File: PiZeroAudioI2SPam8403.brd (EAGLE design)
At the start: 65.1 x 30.2 mm, 60 parts, among them CON1 RPI-ZERO, J1 GROVE, J2 2X2HEADER, J3 JST, J4 AMP FCI 10103594-0001LF, J5 2X1-LOCKING, J6 GROVE, J7 4X1-LOCKING, Q1 DMG2305UX, U1 TXB0104PWR, U2 LSM6DS33, U3 PCM5101A, U4 MCP73831, U5 DMMT5401, U6 TXS0102, U7 PAM8403, U8 PAM2401

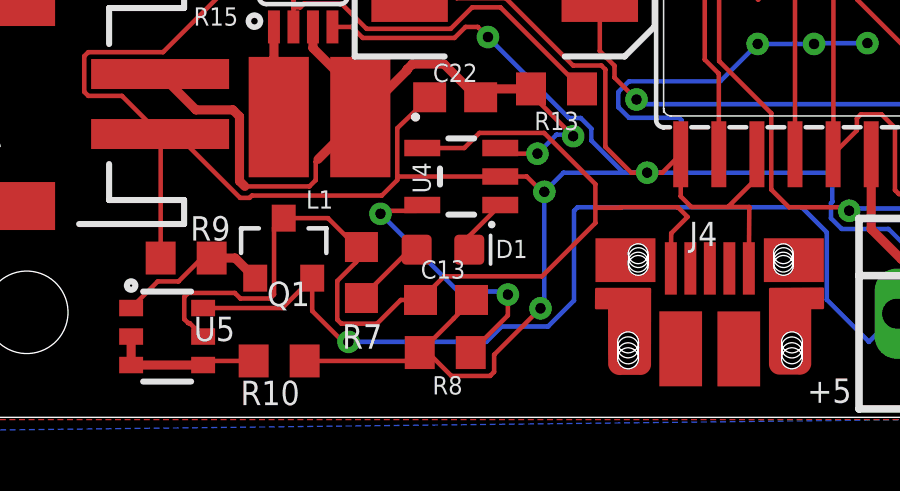
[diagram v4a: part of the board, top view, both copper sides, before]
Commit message: Updated Capacitor footprint
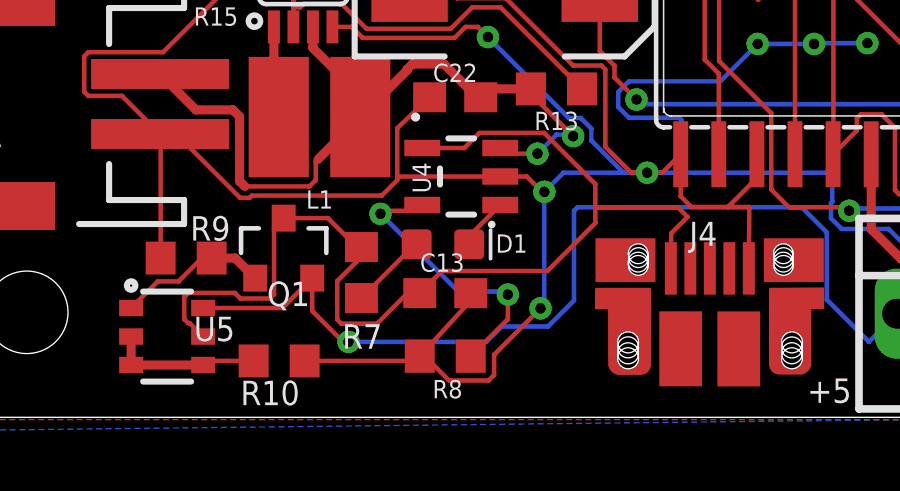
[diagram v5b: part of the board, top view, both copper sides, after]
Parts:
- C13: device SparkFun-Capacitors:0603 -> rcl:C0603
- moved C13 0.23 mm to (-61.3, 5.41)
- moved D1 0.18 mm to (-61.4, 7.04)
- moved R8 0.13 mm to (-61.3, 3.30)
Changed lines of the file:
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@@
 <attribute name="VALUE" x="-56.6928" y="17.6276" size="1.27" layer="27"/>
 </element>
-<element name="C13" library="SparkFun-Capacitors" package="0603" value="4.7uF" x="-61.2648" y="5.1816" smashed="yes">
-<attribute name="NAME" x="-61.3664" y="5.8928" size="0.6096" layer="25" ratio="20" align="bottom-center"/>
-<attribute name="PROD_ID" value="CAP-08280" x="-82.2706" y="27.7622" size="1.778" layer="27" display="off"/>
-<attribute name="VALUE" x="-61.2648" y="4.4196" size="0.6096" layer="27" font="vector" ratio="20" align="top-center"/>
+<element name="C13" library="rcl" library_urn="urn:adsk.eagle:library:334" package="C0603" package3d_urn="urn:adsk.eagle:package:23616/2" value="4.7uF" x="-61.2902" y="5.4102" smashed="yes">
+<attribute name="NAME" x="-61.3918" y="6.1214" size="0.6096" layer="25" ratio="20" align="bottom-center"/>
+<attribute name="SPICEPREFIX" value="C" x="-61.2902" y="5.4102" size="1.778" layer="27" display="off"/>
 </element>
-<element name="D1" library="SparkFun-LED" package="LED-0603" value="BLUE" x="-61.3664" y="6.858" smashed="yes">
-<attribute name="NAME" x="-59.0804" y="6.5786" size="0.6096" layer="25" ratio="20" align="bottom-center"/>
-<attribute name="PROD_ID" value="DIO-08575" x="-73.9902" y="26.8732" size="1.778" layer="27" display="off"/>
-<attribute name="VALUE" x="-61.3664" y="6.223" size="0.6096" layer="27" font="vector" ratio="20" align="top-center"/>
+<element name="D1" library="SparkFun-LED" package="LED-0603" value="BLUE" x="-61.3664" y="7.0358" smashed="yes">
+<attribute name="NAME" x="-59.0804" y="6.7564" size="0.6096" layer="25" ratio="20" align="bottom-center"/>
+<attribute name="PROD_ID" value="DIO-08575" x="-73.9902" y="27.051" size="1.778" layer="27" display="off"/>
+<attribute name="VALUE" x="-61.3664" y="6.4008" size="0.6096" layer="27" font="vector" ratio="20" align="top-center"/>
 </element>
 <element name="R7" library="adafruit" package="R0603" value="1k" x="-64.0842" y="6.096" smashed="yes" rot="R90">
 <attribute name="NAME" x="-64.0588" y="4.3688" size="0.8128" layer="25" ratio="20" rot="R180" align="bottom-center"/>
 </element>
-<element name="R8" library="adafruit" package="R0603" value="2.0k" x="-61.2902" y="3.429" smashed="yes" rot="R180">
-<attribute name="NAME" x="-61.214" y="2.6416" size="0.6096" layer="25" ratio="20" rot="R180" align="bottom-center"/>
+<element name="R8" library="adafruit" package="R0603" value="2.0k" x="-61.2902" y="3.302" smashed="yes" rot="R180">
+<attribute name="NAME" x="-61.214" y="2.5146" size="0.6096" layer="25" ratio="20" rot="R180" align="bottom-center"/>
 </element>
 <element name="U4" library="SparkFun-IC-Power" package="SOT23-5" value="MCP73831" x="-60.7568" y="9.2964" smashed="yes" rot="R90">
@@
 <wire x1="-62.8904" y1="9.1763125" x2="-63.4053125" y2="8.6614" width="0.1524" layer="1"/>
 <wire x1="-63.4053125" y1="8.6614" x2="-67.73563125" y2="8.6614" width="0.1524" layer="1"/>
-<wire x1="-60.4148" y1="5.1816" x2="-60.5434125" y2="5.0470875" width="0.1524" layer="1"/>
-<wire x1="-60.5434125" y1="5.0470875" x2="-61.0076375" y2="4.5615625" width="0.1524" layer="1"/>
-<wire x1="-61.0076375" y1="4.5615625" x2="-62.1402" y2="3.429" width="0.1524" layer="1"/>
-<wire x1="-60.4148" y1="5.1816" x2="-60.5434125" y2="5.0529875" width="0.1524" layer="1"/>
-<wire x1="-60.5434125" y1="5.0529875" x2="-60.5434125" y2="5.0470875" width="0.1524" layer="1"/>
-<wire x1="-65.9774" y1="3.1496" x2="-62.4196" y2="3.1496" width="0.1524" layer="1"/>
-<wire x1="-62.4196" y1="3.1496" x2="-62.1402" y2="3.429" width="0.1524" layer="1"/>
+<wire x1="-60.5434125" y1="5.0470875" x2="-60.579865625" y2="5.0089625" width="0.1524" layer="1"/>
+<wire x1="-60.579865625" y1="5.0089625" x2="-62.1402" y2="3.302" width="0.1524" layer="1"/>
+<wire x1="-60.4402" y1="5.4102" x2="-60.5434125" y2="5.3069875" width="0.1524" layer="1"/>
+<wire x1="-60.5434125" y1="5.3069875" x2="-60.5434125" y2="5.0470875" width="0.1524" layer="1"/>
+<wire x1="-65.9774" y1="3.1496" x2="-62.2926" y2="3.1496" width="0.1524" layer="1"/>
+<wire x1="-62.2926" y1="3.1496" x2="-62.1402" y2="3.302" width="0.1524" layer="1"/>
 <wire x1="-59.4567" y1="9.2964" x2="-62.865" y2="9.2964" width="0.1524" layer="1"/>
 <wire x1="-62.865" y1="9.2964" x2="-62.8904" y2="9.271" width="0.1524" layer="1"/>
@@
 <wire x1="-55.9532" y1="12.8628875" x2="-55.9532" y2="10.284" width="0.1524" layer="1"/>
 <via x="-58.1152" y="4.9022" extent="1-16" drill="0.35"/>
-<wire x1="-61.0848875" y1="2.6496" x2="-59.7955125" y2="2.6496" width="0.1524" layer="1"/>
-<wire x1="-59.7955125" y1="2.6496" x2="-59.6616" y2="2.7835125" width="0.1524" layer="1"/>
-<wire x1="-62.1402" y1="3.429" x2="-61.8642875" y2="3.429" width="0.1524" layer="1"/>
-<wire x1="-59.6616" y1="2.7835125" x2="-59.6616" y2="3.3558" width="0.1524" layer="1"/>
-<wire x1="-61.8642875" y1="3.429" x2="-61.0848875" y2="2.6496" width="0.1524" layer="1"/>
+<wire x1="-61.1610875" y1="2.4972" x2="-59.8463125" y2="2.4972" width="0.1524" layer="1"/>
+<wire x1="-59.8463125" y1="2.4972" x2="-59.6616" y2="2.6819125" width="0.1524" layer="1"/>
+<wire x1="-62.1402" y1="3.302" x2="-61.9658875" y2="3.302" width="0.1524" layer="1"/>
+<wire x1="-59.6616" y1="2.6819125" x2="-59.6616" y2="3.3558" width="0.1524" layer="1"/>
+<wire x1="-61.9658875" y1="3.302" x2="-61.1610875" y2="2.4972" width="0.1524" layer="1"/>
 <wire x1="-59.6616" y1="3.3558" x2="-58.1152" y2="4.9022" width="0.1524" layer="1"/>
 <wire x1="-58.1152" y1="4.9022" x2="-57.9882" y2="5.0292" width="0.1524" layer="16"/>
@@
 <wire x1="-59.2074" y1="5.366653125" x2="-59.202946875" y2="5.3622" width="0.1524" layer="16"/>
 <via x="-59.202946875" y="5.3622" extent="1-16" drill="0.35"/>
-<wire x1="-59.202946875" y1="5.3622" x2="-59.202946875" y2="4.666253125" width="0.1524" layer="1"/>
-<wire x1="-59.202946875" y1="4.666253125" x2="-60.4402" y2="3.429" width="0.1524" layer="1"/>
+<wire x1="-59.202946875" y1="5.3622" x2="-59.202946875" y2="4.539253125" width="0.1524" layer="1"/>
+<wire x1="-59.202946875" y1="4.539253125" x2="-60.4402" y2="3.302" width="0.1524" layer="1"/>
 <wire x1="-62.2499" y1="8.1534" x2="-63.3504" y2="8.1534" width="0.1524" layer="1"/>
 </signal>
@@
 <contactref element="D1" pad="C"/>
 <wire x1="-59.4567" y1="8.3464" x2="-60.4894" y2="7.3137" width="0.1524" layer="1"/>
-<wire x1="-60.4894" y1="7.3137" x2="-60.4894" y2="6.858" width="0.1524" layer="1"/>
+<wire x1="-60.4894" y1="7.3137" x2="-60.4894" y2="7.0358" width="0.1524" layer="1"/>
 </signal>
 <signal name="EN">
@@
 <contactref element="R7" pad="1"/>
 <contactref element="D1" pad="A"/>
-<wire x1="-62.2434" y1="6.858" x2="-62.4722" y2="6.858" width="0.1524" layer="1"/>
-<wire x1="-62.4722" y1="6.858" x2="-64.0842" y2="5.246" width="0.1524" layer="1"/>
+<wire x1="-62.2434" y1="7.0358" x2="-62.2944" y2="7.0358" width="0.1524" layer="1"/>
+<wire x1="-62.2944" y1="7.0358" x2="-64.0842" y2="5.246" width="0.1524" layer="1"/>
 </signal>
 <signal name="+5VCHARGE">
@@
 <wire x1="-64.889" y1="4.5251125" x2="-64.889" y2="5.8144875" width="0.1524" layer="1"/>
 <wire x1="-64.2561" y1="6.9655" x2="-64.2561" y2="7.1179" width="0.1524" layer="1"/>
-<wire x1="-62.7753125" y1="5.1816" x2="-63.5657125" y2="4.3912" width="0.1524" layer="1"/>
+<wire x1="-62.5467125" y1="5.4102" x2="-63.5657125" y2="4.3912" width="0.1524" layer="1"/>
 <wire x1="-64.889" y1="5.8144875" x2="-64.2561" y2="6.4473875" width="0.1524" layer="1"/>
-<wire x1="-62.1148" y1="5.1816" x2="-62.7753125" y2="5.1816" width="0.1524" layer="1"/>
-<wire x1="-61.3274" y1="5.969" x2="-62.1148" y2="5.1816" width="0.1524" layer="1"/>
-<wire x1="-56.2864" y1="7.747" x2="-58.0644" y2="5.969" width="0.1524" layer="1"/>
-<wire x1="-58.0644" y1="5.969" x2="-61.3274" y2="5.969" width="0.1524" layer="1"/>
+<wire x1="-62.1402" y1="5.4102" x2="-62.5467125" y2="5.4102" width="0.1524" layer="1"/>
+<wire x1="-61.4036" y1="6.1468" x2="-62.1402" y2="5.4102" width="0.1524" layer="1"/>
+<wire x1="-56.2864" y1="7.747" x2="-57.8866" y2="6.1468" width="0.1524" layer="1"/>
+<wire x1="-57.8866" y1="6.1468" x2="-61.4036" y2="6.1468" width="0.1524" layer="1"/>
 <wire x1="-62.0569" y1="10.2464" x2="-60.6549875" y2="10.2464" width="0.1524" layer="1"/>
 <wire x1="-60.6549875" y1="10.2464" x2="-60.1513875" y2="10.75" width="0.1524" layer="1"/>

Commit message: Changed Current Resistor to 100K
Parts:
- R15: value DNP -> 100K
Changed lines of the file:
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@@
 <attribute name="NAME" x="-67.2084" y="19.1516" size="0.6096" layer="25" ratio="20" align="bottom-center"/>
 </element>
-<element name="R15" library="adafruit" package="R0603" value="DNP" x="-68.4276" y="16.5608" smashed="yes" rot="R90">
+<element name="R15" library="adafruit" package="R0603" value="100K" x="-68.4276" y="16.5608" smashed="yes" rot="R90">
 <attribute name="NAME" x="-68.9356" y="14.9352" size="0.6096" layer="25" ratio="20" rot="R180" align="bottom-center"/>
 </element>

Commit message: Made Values consistent with Upper case K
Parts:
- R14: value 100k -> 100K
- R7: value 1k -> 1K
- R8: value 2.0k -> 2K
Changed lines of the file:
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@@
 <attribute name="VALUE" x="-61.3664" y="6.4008" size="0.6096" layer="27" font="vector" ratio="20" align="top-center"/>
 </element>
-<element name="R7" library="adafruit" package="R0603" value="1k" x="-64.0842" y="6.096" smashed="yes" rot="R90">
+<element name="R7" library="adafruit" package="R0603" value="1K" x="-64.0842" y="6.096" smashed="yes" rot="R90">
 <attribute name="NAME" x="-64.0588" y="4.3688" size="0.8128" layer="25" ratio="20" rot="R180" align="bottom-center"/>
 </element>
-<element name="R8" library="adafruit" package="R0603" value="2.0k" x="-61.2902" y="3.302" smashed="yes" rot="R180">
+<element name="R8" library="adafruit" package="R0603" value="2K" x="-61.2902" y="3.302" smashed="yes" rot="R180">
 <attribute name="NAME" x="-61.214" y="2.5146" size="0.6096" layer="25" ratio="20" rot="R180" align="bottom-center"/>
 </element>
@@
 <attribute name="NAME" x="-63.119" y="18.4404" size="0.6096" layer="25" ratio="20" align="bottom-center"/>
 </element>
-<element name="R14" library="adafruit" package="R0603" value="100k" x="-67.5386" y="20.3962" smashed="yes">
+<element name="R14" library="adafruit" package="R0603" value="100K" x="-67.5386" y="20.3962" smashed="yes">
 <attribute name="NAME" x="-67.2084" y="19.1516" size="0.6096" layer="25" ratio="20" align="bottom-center"/>
 </element>

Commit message: Changed the name of RPI Header
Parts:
- CON1: value RPI-ZERO -> RPI-Header
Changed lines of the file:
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@@
 </autorouter>
 <elements>
-<element name="CON1" library="RPI-Zero" package="RASPBERRYPI_BASTELSTUBE_V13_RASPI_BOARD_B+_FULL" value="RPI-ZERO" x="-78.74" y="1.27"/>
+<element name="CON1" library="RPI-Zero" package="RASPBERRYPI_BASTELSTUBE_V13_RASPI_BOARD_B+_FULL" value="RPI-Header" x="-78.74" y="1.27"/>
 <element name="U2" library="HappyBrackets" library_urn="urn:adsk.eagle:library:5224691" package="LGA-16-3X3" package3d_urn="urn:adsk.eagle:package:5224694/1" value="LSM6DS33" x="-63.7924" y="22.733" smashed="yes" rot="R270">
 <attribute name="NAME" x="-63.627" y="20.5102" size="0.6096" layer="25" ratio="20" align="bottom-center"/>
